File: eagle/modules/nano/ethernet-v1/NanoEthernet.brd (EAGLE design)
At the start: 113 x 82.5 mm, 55 parts, among them IC1 ULN2803A, IC2 ULN2803A, IC4 ULN2803A, J1 RJ12STRAIGHT-RS232-SERVER

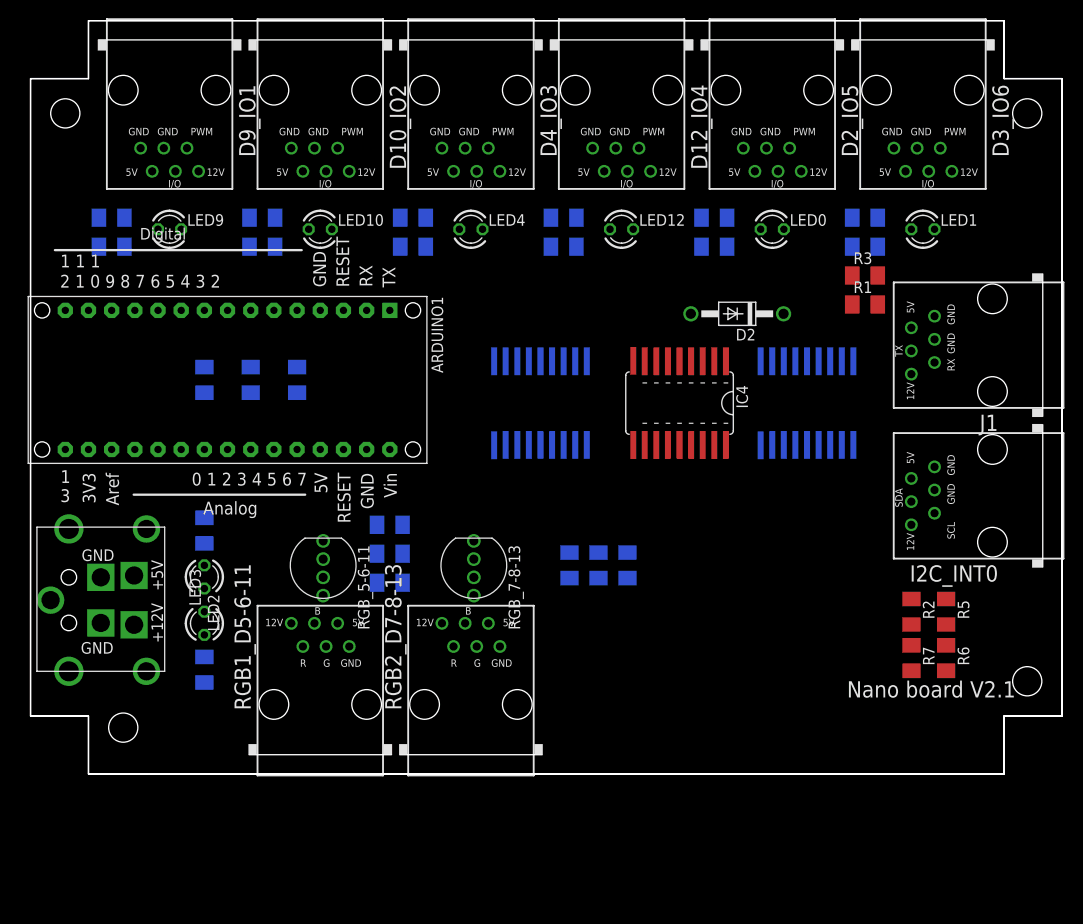
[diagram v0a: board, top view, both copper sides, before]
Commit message: New NanoEthernet version (draft)
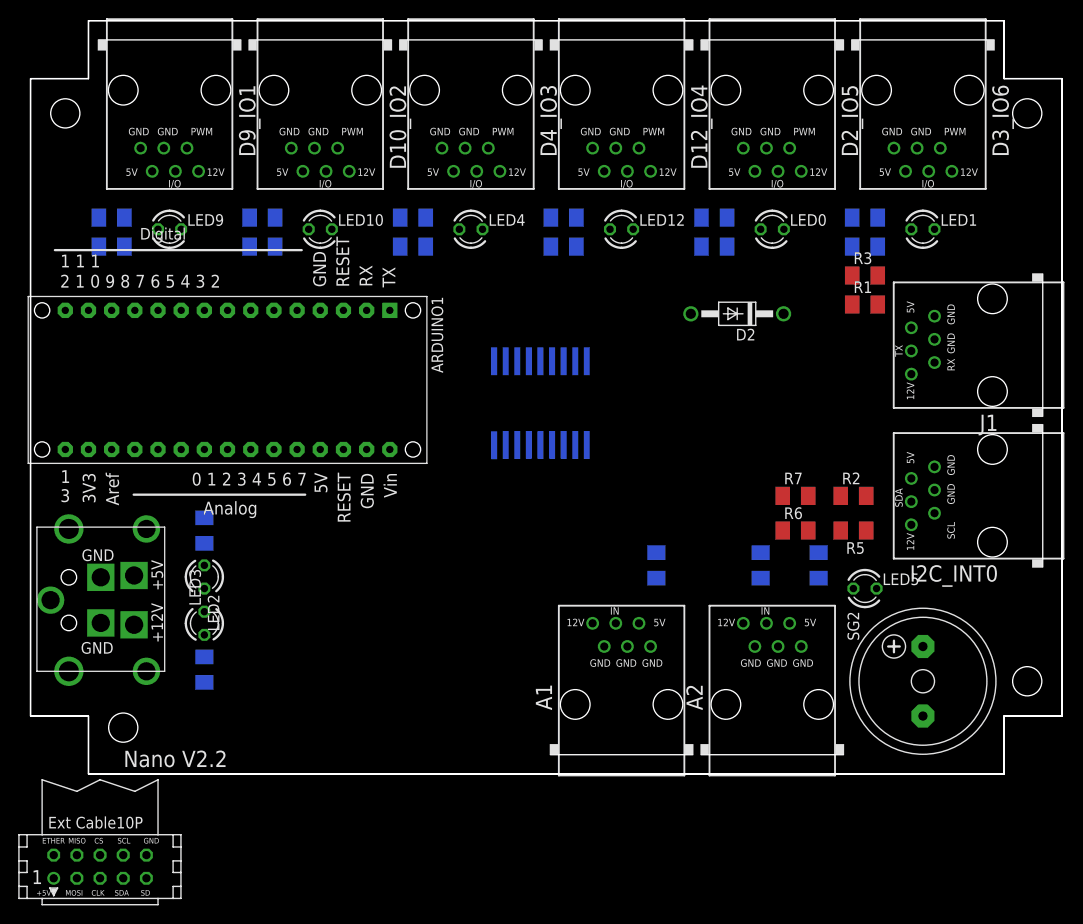
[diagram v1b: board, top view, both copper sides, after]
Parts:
- removed IC1, IC4: ULN2803A, lpatiny:SO18W
- removed RA3, RA6, RA7: 10K, resistor:M1206
- removed RGB1_D5-6-11: RGB1, lpatiny:RJ12-STRAIGHT-RGB@1
- removed RGB2_D7-8-13: RGB2, lpatiny:RJ12-STRAIGHT-RGB@1
- removed RGB_5-6-11, RGB_7-8-13: (no value), lpatiny:LED-TRICOLOR-THROUGHHOLE
- removed RL11, RL13, RL5, RL6, RL7, RL8: 1K, resistor:M1206
- added A1, A2: RJ12STRAIGHT-ANALOG, lpatiny:RJ12-STRAIGHT-ANALOG
- added CON1: (no value), lpatiny:CON10EXT
- added LED5: (no value), lpatiny:LED3MM
- added RA0, RA1, RL14: 1K, resistor:M1206
- added SG2: F/HMB, buzzer:F/HMB
- moved R7 21.8 mm to (82.5, 30.5), turned to 0 degrees
- moved R6 21.6 mm to (82.5, 26.7), turned to 0 degrees
- moved R2 14.2 mm to (88.9, 30.5), turned to 0 degrees
- moved R5 13.5 mm to (88.9, 26.7), turned to 180 degrees
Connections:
- removed net N$1: RGB_5-6-11.RED, RL5.2
- removed net N$11: RGB_7-8-13.BLU, RL8.2
- removed net N$14: RGB_7-8-13.GRN, RL13.2
- removed net N$17: IC4.13, IC4.14, RGB1_D5-6-11.G, RL11.1
- removed net N$19: IC4.11, IC4.12, RGB2_D7-8-13.R, RL7.1
- removed net N$2: RGB_5-6-11.BLU, RL6.2
- removed net N$29: IC1.15, IC1.16, RGB2_D7-8-13.G, RL13.1
- removed net N$3: IC1.17, IC1.18, RGB2_D7-8-13.B, RL8.1
- removed net N$4: RGB_5-6-11.GRN, RL11.2
- removed net N$5: IC4.17, IC4.18, RGB1_D5-6-11.R, RL5.1
- removed net N$6: IC4.15, IC4.16, RGB1_D5-6-11.B, RL6.1
- removed net N$9: RGB_7-8-13.RED, RL7.2
- new net D2B8: A1.IN, RA0.1
- new net D2B9: A2.IN, RA1.1
- new net N$10: LED5.A, RL14.1
- net +12V: now also A1.+12V, A2.+12V; no longer RGB1_D5-6-11.+12V, RGB2_D7-8-13.+12V
- net +5V: now also A1.+5V, A2.+5V; no longer RGB1_D5-6-11.+5V, RGB2_D7-8-13.+5V, RGB_5-6-11.GND, RGB_7-8-13.GND
- net A1: now also RA0.2
- net A2: now also RA1.2
- net COM: no longer IC1.10, IC4.10
- net D11: no longer IC4.1, IC4.2
- net D13: no longer IC1.3, IC1.4
- net D2: no longer IC1.5, IC1.6
- net D3: no longer IC1.7, IC1.8
- net D4: no longer IC2.1, IC2.2
- net D5: no longer IC4.5, IC4.6
- net D6: no longer IC4.3, IC4.4
- net D7: no longer IC4.7, IC4.8
- net D8: no longer IC1.1, IC1.2
- net D9: no longer IC2.3, IC2.4
- net GND: now also A1.GND1, A1.GND2, A1.GND3, A2.GND1, A2.GND2, A2.GND3, LED5.K, SG2.-; no longer IC1.9, IC4.9, RA3.2, RA6.2, RA7.2, RGB1_D5-6-11.GND1, RGB2_D7-8-13.GND1
- net N$16: no longer RA3.1
- net N$18: now also IC2.16; no longer IC2.17, IC2.18
- net N$20: now also RL14.2; no longer RA6.1
- net N$22: now also SG2.+; no longer RA7.1
- net N$35: now also IC2.17; no longer IC1.11, IC1.12
- net N$40: no longer IC1.13, IC1.14
- net N$42: no longer IC2.16
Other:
- board text added: "Nano V2.2"
- board text removed: "Nano board V2.1"

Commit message: update ethernet card
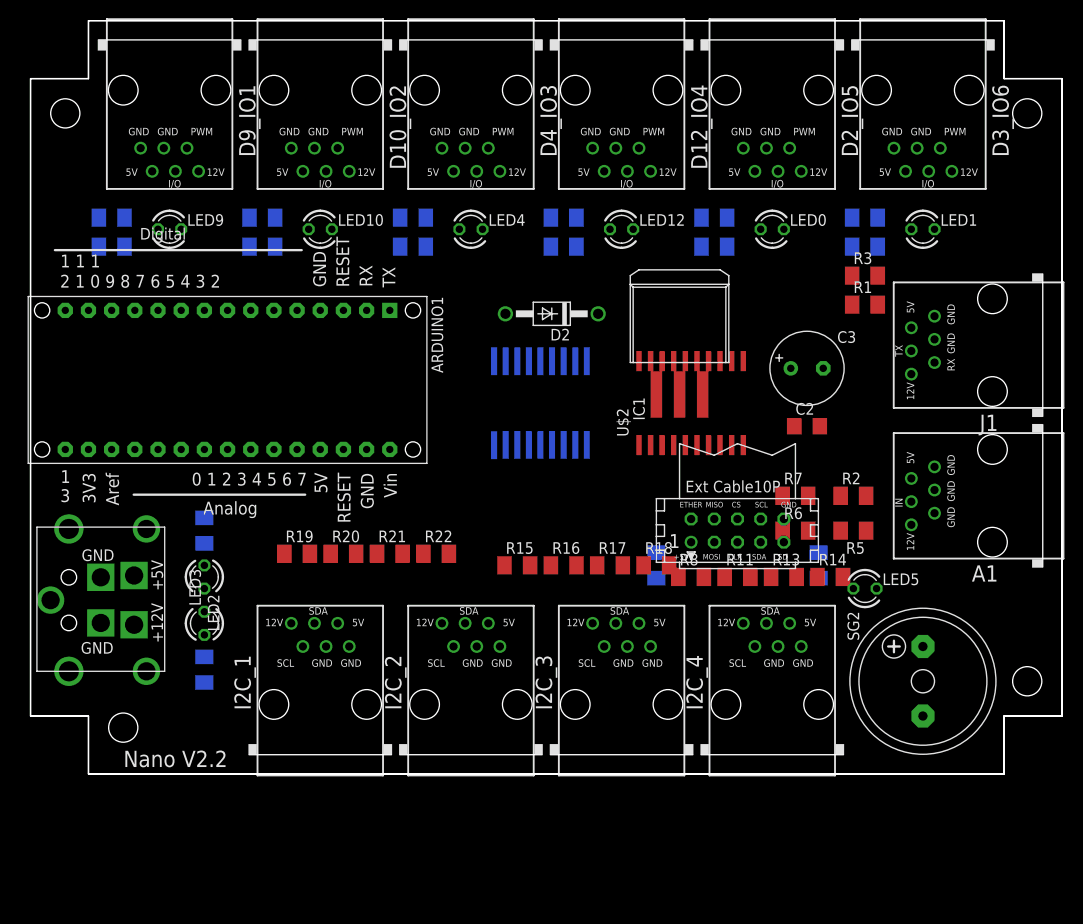
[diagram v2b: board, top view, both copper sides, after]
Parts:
- removed A2: RJ12STRAIGHT-ANALOG, lpatiny:RJ12-STRAIGHT-ANALOG
- removed I2C_INT0: I2C, lpatiny:RJ12-STRAIGHT-I2C@1
- removed RA1: 1K, resistor:M1206
- added C2: 0.47uF, rcl:C1206
- added C3: 33uF, rcl:E3,5-8
- added I2C_1, I2C_2, I2C_4: I2C, lpatiny:RJ12-STRAIGHT-I2C
- added I2C_3: I2C, lpatiny:RJ12-STRAIGHT-I2C@1
- added IC1: LM3940IS-3.3F, lpatiny:DD-3
- added R11, R15, R16, R19, R20, R8: 1K, resistor:M1206
- added R13, R14, R17, R18, R21, R22: 10K, resistor:M1206
- added U$2: PCA9518, lpatiny:SO20W
- moved CON1 79.0 mm to (76.2, 26.7)
- moved A1 46.6 mm to (104.1, 30.5), turned to 90 degrees
- moved D2 20.3 mm to (55.8, 50.4)
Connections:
- removed net D2B9: A2.IN, RA1.1
- new net +3V3: C3.+, IC1.3, U$2.20
- new net D2B10: I2C_4.SDA, R8.1
- new net D2B11: I2C_2.SDA, R15.1
- new net D2B12: I2C_1.SDA, R19.1
- new net N$1: I2C_4.SCL, R11.1
- new net N$11: I2C_1.SCL, R20.1
- new net N$14: R20.2, R21.1, U$2.5
- new net N$17: R19.2, R22.1, U$2.6
- new net N$2: R11.2, R13.1, U$2.15
- new net N$3: R14.1, R8.2, U$2.16
- new net N$5: I2C_2.SCL, R16.1
- new net N$6: R16.2, R17.1, U$2.8
- new net N$9: R15.2, R18.1, U$2.9
- net +12V: now also I2C_1.+12V, I2C_2.+12V, I2C_3.+12V, I2C_4.+12V; no longer A2.+12V, I2C_INT0.+12V
- net +5V: now also C2.1, I2C_1.+5V, I2C_2.+5V, I2C_3.+5V, I2C_4.+5V, IC1.1, R13.2, R14.2, R17.2, R18.2, R21.2, R22.2; no longer A2.+5V, I2C_INT0.+5V
- net A2: no longer RA1.2
- net D2B4: now also I2C_3.SDA; no longer I2C_INT0.SDA
- net GND: now also C2.2, C3.-, I2C_1.GND1, I2C_1.GND2, I2C_2.GND1, I2C_2.GND2, I2C_3.GND1, I2C_3.GND2, I2C_4.GND1, I2C_4.GND2, IC1.2, U$2.10; no longer A2.GND1, A2.GND2, A2.GND3, I2C_INT0.GND1, I2C_INT0.GND2
- net N$8: now also I2C_3.SCL; no longer I2C_INT0.SCL
- net SCL: now also U$2.12, U$2.3
- net SDA: now also U$2.13, U$2.4
